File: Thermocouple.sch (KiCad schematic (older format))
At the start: 15 parts

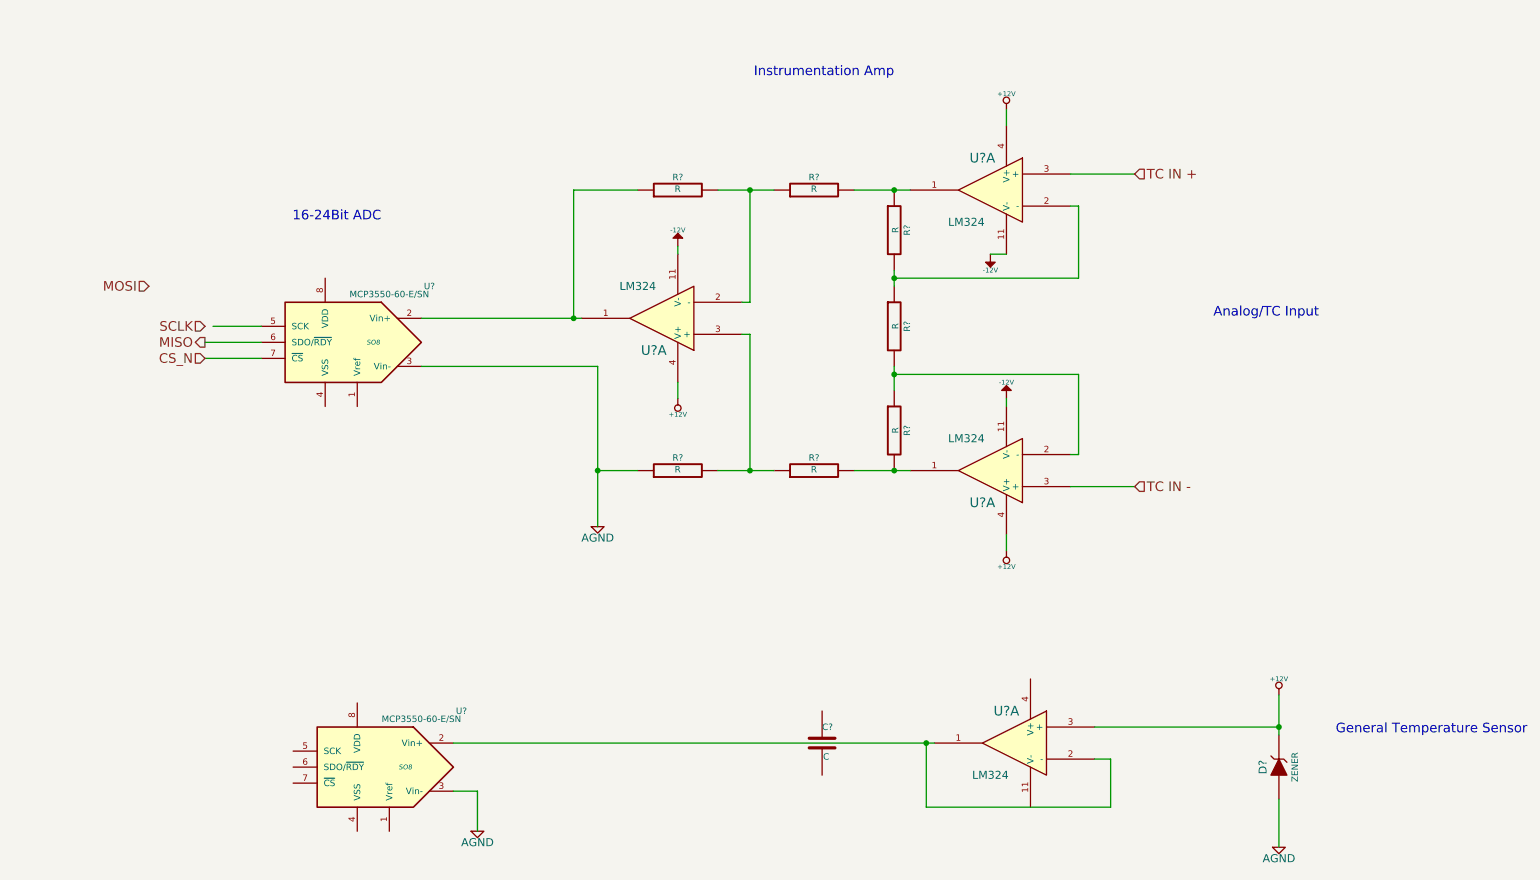
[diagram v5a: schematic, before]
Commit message: Preliminary Module Layouts
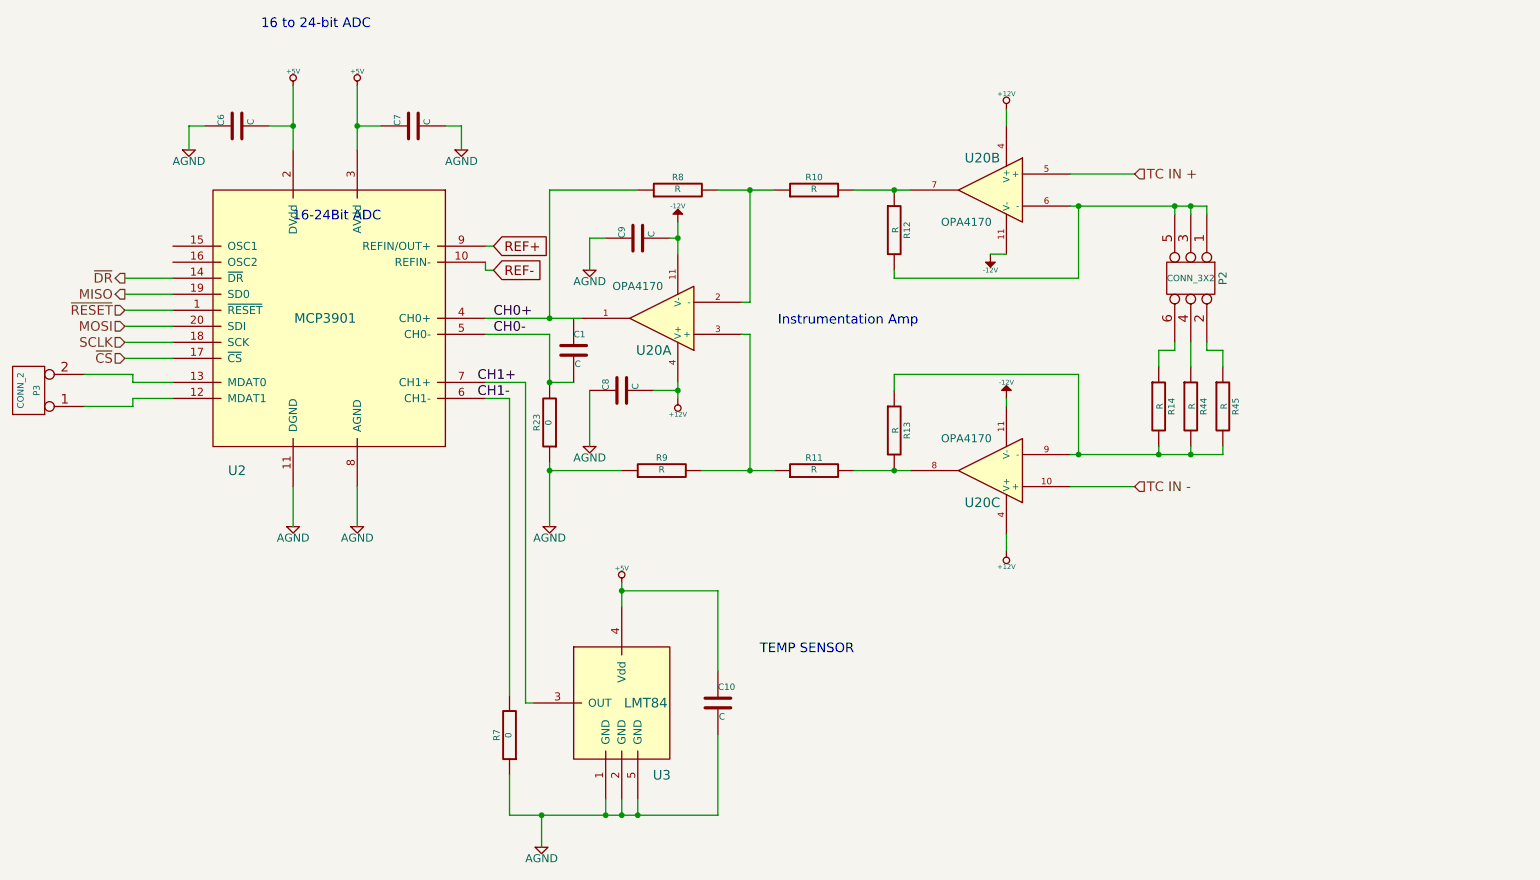
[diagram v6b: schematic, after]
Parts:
- removed D?: ZENER, ~, symbol ZENER
- removed U?: LM324, ~, symbol LM324
- removed U? (x2): MCP3550-60-E/SN, SO8, symbol MCP3550-60-E/SN
- added C10, C6, C7, C8, C9: C, ~, symbol C
- added P2: CONN_3X2, symbol CONN_3X2
- added P3: CONN_2, symbol CONN_2
- added R14, R44: R, ~, symbol R
- added R23, R7: 0, ~, symbol R
- added U2: MCP3901, symbol MCP3901
- added U3: LMT84, symbol LMT84
- U20: renamed from U?; value LM324 -> OPA4170
- gave numbers to parts that had none: 8
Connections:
- net +12V: now also C8.2
- net -12V: now also C9.2
- net AGND: now also C10.2, C6.1, C7.2, C8.1, C9.1, R23.1, R7.1, U2.11 (DGND), U2.8 (AGND), U3.1 (GND), U3.2 (GND), U3.5 (GND)
- net MISO: now also U2.19 (SD0)
- net MOSI: now also U2.20 (SDI)
- net SCLK: now also U2.18 (SCK)
- net TC IN +: now also U20.5 (+); no longer U20.3 (+)
- net TC IN -: now also U20.10 (+); no longer U20.3 (+)
- net at R10.2, R12.1: now also U20.7; no longer U20.1
- net at R11.2, R13.2: now also U20.8; no longer U20.1
- net at R13.1, R45.2: now also U20.9 (-), R14.2, R44.2; no longer U20.2 (-)
- net CH0+: now reaches R8.1, U20.1
- net CH0+: now also U2.4 (CH0+)
- net CH0-: now reaches C1.2
- net CH0-: now also R23.2, U2.5 (CH0-)
- new net: P2.1, P2.3, P2.5, R12.2, U20.6 (-)
- new net: P2.2, R45.1
- new net: P3.1 (P1), U2.12 (MDAT1)
- new net: P3.2 (PM), U2.13 (MDAT0)
- new net: R7.2, U2.6 (CH1-)
- new net: U2.7 (CH1+), U3.3 (OUT)
- new net: P2.6, R14.1
- new net: P2.4, R44.1
- new net +5V: C10.1, C6.2, C7.1, U2.2 (DVdd), U2.3 (AVdd), U3.4 (Vdd)
- new net REF+: U2.9 (REFIN/OUT+)
- new net REF-: U2.10 (REFIN-)
- new net ~CS: U2.17 (~CS)
- new net ~DR: U2.14 (~DR)
- new net ~RESET: U2.1 (~RESET)
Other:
- note added: "16 to 24-bit ADC"
- note added: "TEMP SENSOR\n"
- note removed: "Analog/TC Input"
- note removed: "General Temperature Sensor\n"
- moved on the sheet: C1, R45, R9
